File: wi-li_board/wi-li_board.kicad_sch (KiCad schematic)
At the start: 30 parts, among them J1 Barrel_Jack_MountingPin, J2 2059-302/998-403, J3 2059-302/998-403, J4 2059-302/998-403, Q1 Q_NMOS_DGS, Q2 Q_NMOS_DGS, Q3 Q_NMOS_DGS, U1 AP1509, U2 ESP-12E

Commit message: fix issues from first rev
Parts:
- removed R1: 10k, Resistor_SMD:R_0805_2012Metric_Pad1.20x1.40mm_HandSolder, symbol Device:R_Small_US
- removed U2: ESP-12E, RF_Module:ESP-12E, symbol ESP8266:ESP-12E
- added R3, R6, R7, R8: 10k, Resistor_SMD:R_0805_2012Metric_Pad1.20x1.40mm_HandSolder, symbol Device:R_Small_US
- added U2: ESP-12E, RF_Module:ESP-12E, symbol RF_Module:ESP-12E
- L1: footprint Inductor_SMD:L_Vishay_IFSC-1515AH_4x4x1.8mm -> RLC:L_Vishay_IFSC-1515AH_HandSolder
- Q1, Q2, Q3: symbol Device:Q_NMOS_DGS -> Device:Q_NMOS_GSD
- renumbered R3 to R1, R7 to R10, R8 to R11, R6 to R9
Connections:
- net GND: now also Q1.2 (S), Q2.2 (S), Q3.2 (S), R6.1, U2.15 (GND); no longer Q1.3 (S), Q2.3 (S), Q3.3 (S)
- net GPIO_12: now also U2.6 (GPIO12)
- net GPIO_14: now also U2.5 (GPIO14)
- net GPIO_4: now also U2.19 (GPIO4)
- net VDD: now also R3.1, R7.1, R8.1, U2.8 (VCC)
- net at R5.1, R9.2: now also Q2.1 (G); no longer Q2.2 (G)
- net at F4.1: now also Q2.3 (D); no longer Q2.1 (D)
- net at R2.2: now also U2.1 (~{RST})
- net at R1.1, R4.2: now also Q1.1 (G); no longer Q1.2 (G)
- net at F3.1: now also Q1.3 (D); no longer Q1.1 (D)
- net at Q3.1 (G): now also R10.1, R11.2; no longer F5.1
- new net: R6.2, U2.16 (GPIO15)
- new net: R8.2, U2.17 (GPIO2)
- new net: F5.1, Q3.3 (D)
- new net: R7.2, U2.18 (GPIO0)
- new net: R3.2, U2.3 (EN)
- no-connect marks 9 -> 12
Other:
- note removed: "Power: .231W at 70mA"

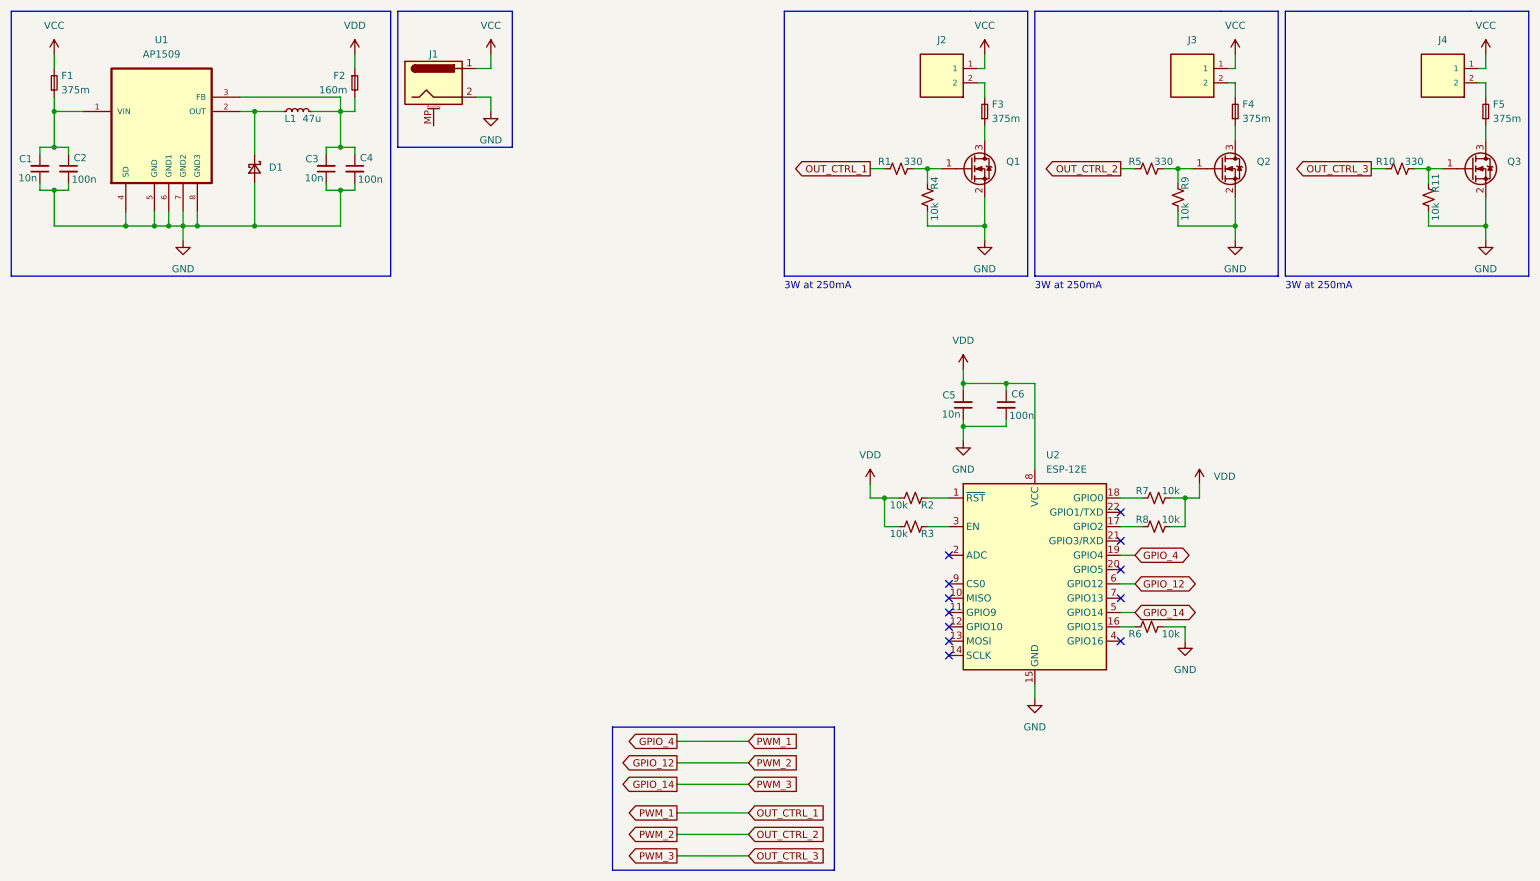
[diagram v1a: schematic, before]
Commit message: add current measurement and do most of the layout, plus fix voltage regulator mistake
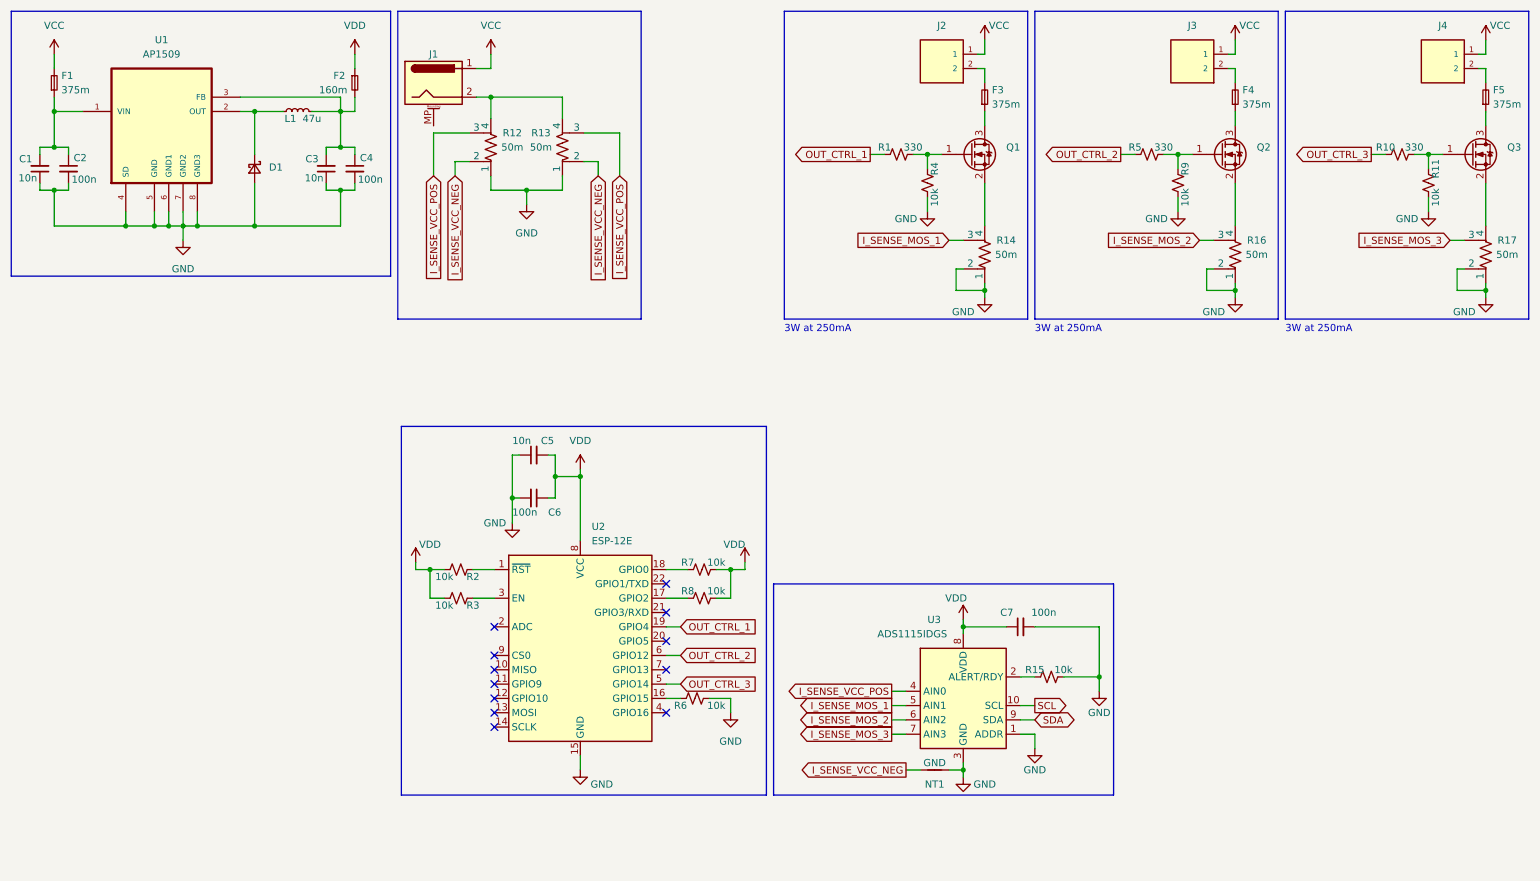
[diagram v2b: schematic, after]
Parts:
- added C7: 100n, Capacitor_SMD:C_0805_2012Metric_Pad1.18x1.45mm_HandSolder, symbol Device:C_Small
- added NT1: GND, symbol Device:NetTie_2
- added R12, R13, R14, R16, R17: 50m, RLC:R_shunt_0805_2012Metric_Pad1.20x1.40mm_HandSolder, symbol Device:R_Shunt_US
- added R15: 10k, Resistor_SMD:R_0805_2012Metric_Pad1.20x1.40mm_HandSolder, symbol Device:R_Small_US
- added U3: ADS1115IDGS, Package_SO:TSSOP-10_3x3mm_P0.5mm, symbol Analog_ADC:ADS1115IDGS
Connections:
- net GND: now also C7.2, NT1.1, R12.1, R13.1, R14.1, R14.2, R15.1, R16.1, R16.2, R17.1, R17.2, U3.1 (ADDR), U3.3 (GND); no longer J1.2, Q1.2 (S), Q2.2 (S), Q3.2 (S)
- net VDD: now also C7.1, U3.8 (VDD)
- net GPIO_12 renamed OUT_CTRL_2
- net GPIO_14 renamed OUT_CTRL_3
- net GPIO_4 renamed OUT_CTRL_1
- new net: Q2.2 (S), R16.4
- new net: Q3.2 (S), R17.4
- new net: J1.2, R12.4, R13.4
- new net: R15.2, U3.2 (ALERT/RDY)
- new net: Q1.2 (S), R14.4
- new net I_SENSE_MOS_1: R14.3, U3.5 (AIN1)
- new net I_SENSE_MOS_2: R16.3, U3.6 (AIN2)
- new net I_SENSE_MOS_3: R17.3, U3.7 (AIN3)
- new net I_SENSE_VCC_NEG: NT1.2, R12.2, R13.2
- new net I_SENSE_VCC_POS: R12.3, R13.3, U3.4 (AIN0)
- new net SCL: U3.10 (SCL)
- new net SDA: U3.9 (SDA)
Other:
- moved on the sheet: F3, F4, F5, J2, J3, J4, Q1, Q2, Q3, R1, R10, R11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

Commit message: Circular Board   - Fix mistake on voltage regulator from previous version   - Add ADC IC   - Add current measurement to all three channels and input using ADC IC   - Add programming header   - Switch to XT-30 connectors instead of Wago   - Panelize
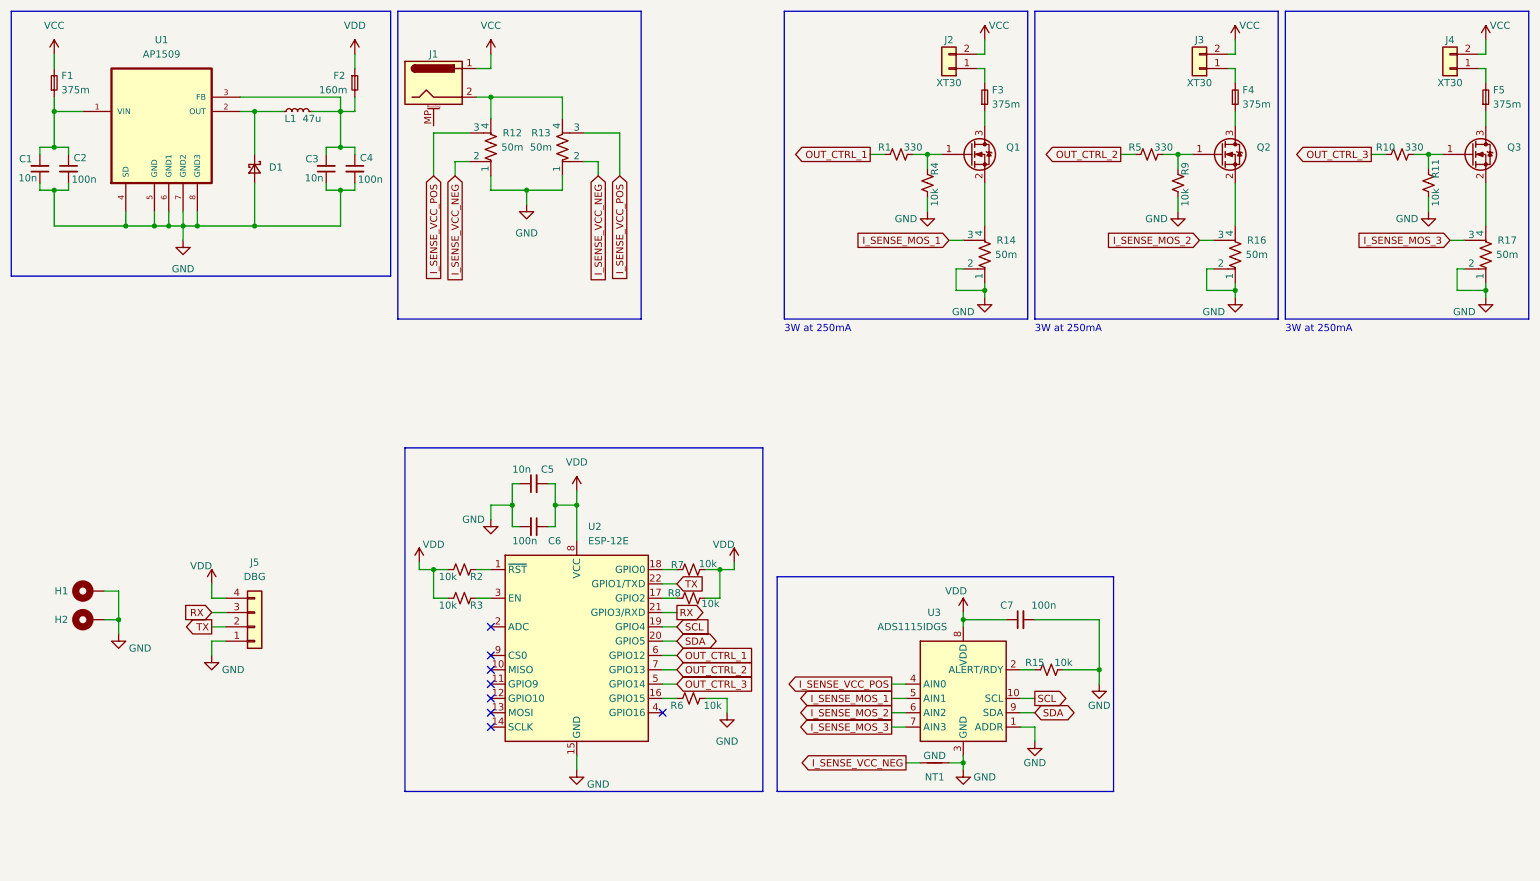
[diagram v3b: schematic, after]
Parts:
- removed J2, J3, J4: 2059-302/998-403, Wago:WAGO_2059-302_998-403, symbol Wago:2059-302/998-403
- added H1, H2: MountingHole_Pad, MountingHole:MountingHole_2.2mm_M2_Pad_Via, symbol Mechanical:MountingHole_Pad
- added J2, J3, J4: XT30, Connector_AMASS:AMASS_XT30U-M_1x02_P5.0mm_Vertical, symbol Connector_Generic:Conn_01x02
- added J5: DBG, Connector_PinHeader_2.54mm:PinHeader_1x04_P2.54mm_Vertical, symbol Connector_Generic:Conn_01x04
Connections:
- net GND: now also H1.1, H2.1, J5.1 (Pin_1)
- net OUT_CTRL_1: now also U2.6 (GPIO12); no longer U2.19 (GPIO4)
- net OUT_CTRL_2: now also U2.7 (GPIO13); no longer U2.6 (GPIO12)
- net SCL: now also U2.19 (GPIO4)
- net SDA: now also U2.20 (GPIO5)
- net VCC: now also J2.2 (Pin_2), J3.2 (Pin_2), J4.2 (Pin_2)
- net VDD: now also J5.4 (Pin_4)
- net at F4.2: now also J3.1 (Pin_1)
- net at F3.2: now also J2.1 (Pin_1)
- net at F5.2: now also J4.1 (Pin_1)
- net RX: now reaches U2.21 (GPIO3/RXD)
- net RX: now also J5.3 (Pin_3)
- net TX: now reaches U2.22 (GPIO1/TXD)
- net TX: now also J5.2 (Pin_2)
- no-connect marks 12 -> 8
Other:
- moved on the sheet: C5, C6, C7, NT1, R15, R2, R3, R6, R7, R8, U2, U3
